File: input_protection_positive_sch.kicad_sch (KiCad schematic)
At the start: 26 parts, among them Q1 SQM120P06, Q2 SQM120P06, U1 ADM1270

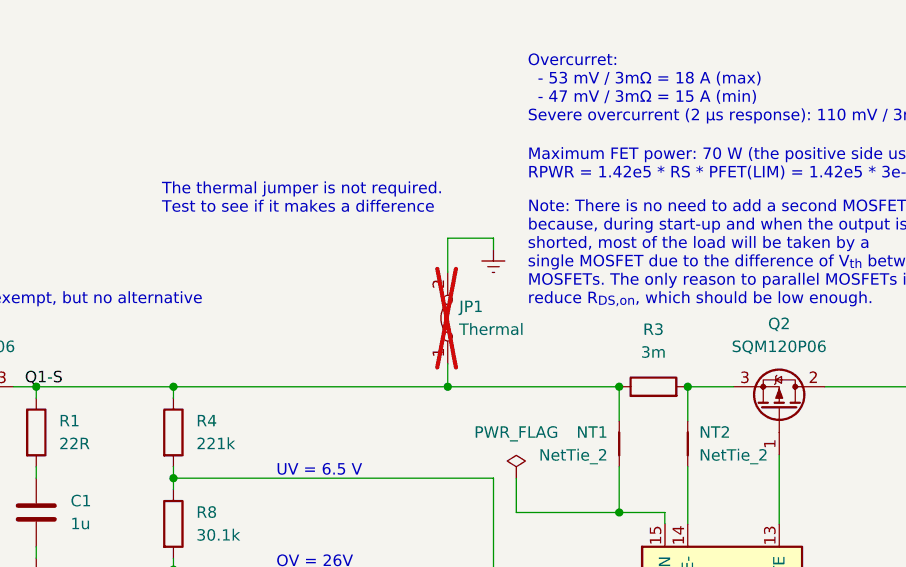
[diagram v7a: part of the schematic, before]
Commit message: Updated layout to improve handling flexing of the PCB Changed MLCCs to flexible termination Removed thermal jumper
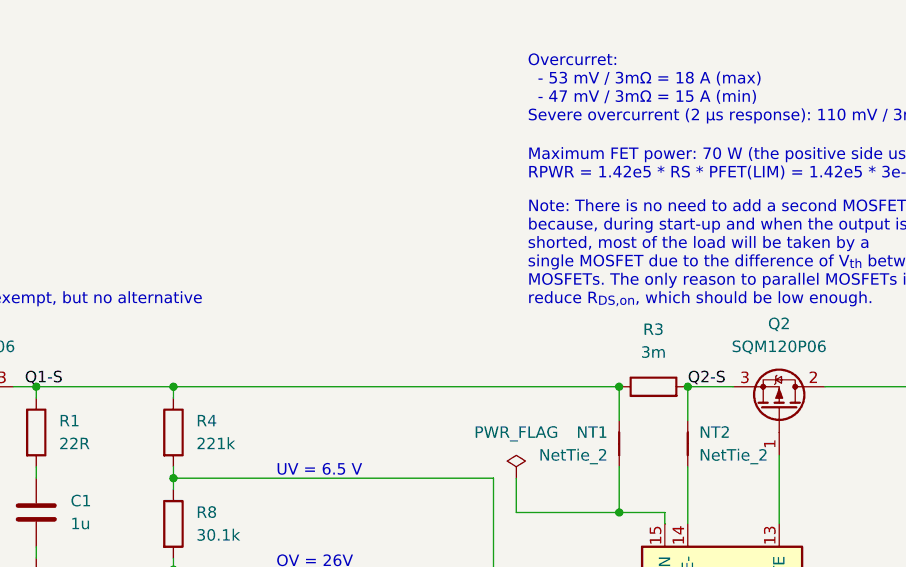
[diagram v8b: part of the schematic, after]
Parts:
- removed JP1: Thermal, Resistor_SMD:R_0612_1632Metric, symbol Jumper:Jumper_2_Bridged
- C1, C14, C15, C3: PN C1206C105K1RACAUTO -> C1206X105K1RACAUTO; digikey# 399-13374-1-ND -> 399-13377-1-ND
- C13: PN C1206C474K1RECAUTO -> C1206X474K1RECAUTO; digikey# 399-C1206C474K1RECAUTOCT-ND -> 399-16438-1-ND
- C2: PN C0805C104K1RACAUTO -> C0805X104K1RACAUTO; digikey# 399-6926-1-ND -> 399-11601-1-ND
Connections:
- net Q2-S: now reaches NT2.2, Q2.3 (S), R3.2
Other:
- note removed: "The thermal jumper is not required. Test to see if it makes a difference"
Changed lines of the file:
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@@
   (junction (at 27.94 64.77) (diameter 0) (color 0 0 0 0)
-  )
-  (junction (at 147.32 64.77) (diameter 0) (color 0 0 0 0)
   )
   (junction (at 163.83 97.79) (diameter 0) (color 0 0 0 0)
@@
     (stroke (width 0) (type default))
   )
-  (wire (pts (xy 116.84 64.77) (xy 147.32 64.77))
-    (stroke (width 0) (type default))
-  )
   (wire (pts (xy 45.72 64.77) (xy 45.72 67.31))
     (stroke (width 0) (type default))
   )
-  (wire (pts (xy 152.4 49.53) (xy 152.4 48.26))
-    (stroke (width 0) (type default))
-  )
   (wire (pts (xy 163.83 97.79) (xy 163.83 100.33))
     (stroke (width 0) (type default))
@@
     (stroke (width 0) (type default))
   )
-  (wire (pts (xy 152.4 48.26) (xy 147.32 48.26))
-    (stroke (width 0) (type default))
-  )
   (wire (pts (xy 245.11 64.77) (xy 259.08 64.77))
     (stroke (width 0) (type default))
@@
     (stroke (width 0) (type default))
   )
-  (wire (pts (xy 147.32 62.23) (xy 147.32 64.77))
-    (stroke (width 0) (type default))
-  )
   (wire (pts (xy 45.72 83.82) (xy 45.72 85.09))
     (stroke (width 0) (type default))
   )
-  (wire (pts (xy 147.32 64.77) (xy 166.37 64.77))
+  (wire (pts (xy 116.84 64.77) (xy 166.37 64.77))
     (stroke (width 0) (type default))
   )
@@
   )
   (wire (pts (xy 205.74 92.71) (xy 205.74 87.63))
-    (stroke (width 0) (type default))
-  )
-  (wire (pts (xy 147.32 48.26) (xy 147.32 52.07))
     (stroke (width 0) (type default))
   )
@@
     (effects (font (size 1.27 1.27)) (justify left bottom))
   )
-  (text "The thermal jumper is not required.\nTest to see if it makes a difference"
-    (at 115.57 45.72 0)
-    (effects (font (size 1.27 1.27)) (justify left bottom))
-  )
   (text "RoHS exempt, but no alternative" (at 91.44 55.88 0)
     (effects (font (size 1.27 1.27)) (justify left bottom))
@@
   )
   (label "Q1-D" (at 82.55 64.77 0) (fields_autoplaced)
+    (effects (font (size 1.27 1.27)) (justify left bottom))
+  )
+  (label "Q2-S" (at 173.99 64.77 0) (fields_autoplaced)
     (effects (font (size 1.27 1.27)) (justify left bottom))
   )
@@
       (effects (font (size 1.27 1.27)) hide)
     )
-    (property "PN" "C1206C105K1RACAUTO" (at 45.72 80.01 0)
+    (property "PN" "C1206X105K1RACAUTO" (at 45.72 80.01 0)
       (effects (font (size 1.27 1.27)) hide)
     )
@@
       (effects (font (size 1.27 1.27)) hide)
     )
-    (property "digikey#" "399-13374-1-ND" (at 45.72 80.01 0)
+    (property "digikey#" "399-13377-1-ND" (at 45.72 80.01 0)
       (effects (font (size 1.27 1.27)) hide)
     )
@@
       (effects (font (size 1.27 1.27)) hide)
     )
-    (property "PN" "C0805C104K1RACAUTO" (at 245.11 74.93 0)
+    (property "PN" "C0805X104K1RACAUTO" (at 245.11 74.93 0)
       (effects (font (size 1.27 1.27)) hide)
     )
@@
       (effects (font (size 1.27 1.27)) hide)
     )
-    (property "digikey#" "399-6926-1-ND" (at 245.11 74.93 0)
+    (property "digikey#" "399-11601-1-ND" (at 245.11 74.93 0)
       (effects (font (size 1.27 1.27)) hide)
     )
@@
     )
   )
-  (symbol (lib_id "power:Earth") (at 152.4 49.53 0) (unit 1)
-    (in_bom yes) (on_board yes) (dnp no) (fields_autoplaced)
-    (property "Reference" "#PWR070" (at 152.4 55.88 0)
-      (effects (font (size 1.27 1.27)) hide)
-    )
-    (property "Value" "Earth" (at 152.4 53.34 0)
-      (effects (font (size 1.27 1.27)) hide)
-    )
-    (property "Footprint" "" (at 152.4 49.53 0)
-      (effects (font (size 1.27 1.27)) hide)
-    )
-    (property "Datasheet" "~" (at 152.4 49.53 0)
-      (effects (font (size 1.27 1.27)) hide)
-    )
-    (pin "1")
-    (instances
-      (project "backplane"
-        (path "/b4ace06a-3ad4-479e-aaa4-d547ecf6903f/f9160387-088e-4a7b-8d58-b2647e07444c"
-          (reference "#PWR070") (unit 1)
-        )
-      )
-    )
-  )
   (symbol (lib_id "Device:R") (at 228.6 72.39 0) (unit 1)
     (in_bom yes) (on_board yes) (dnp no) (fields_autoplaced)
@@
       (effects (font (size 1.27 1.27)) hide)
     )
-    (property "PN" "C1206C105K1RACAUTO" (at 203.2 102.87 0)
+    (property "PN" "C1206X105K1RACAUTO" (at 203.2 102.87 0)
       (effects (font (size 1.27 1.27)) hide)
     )
@@
       (effects (font (size 1.27 1.27)) hide)
     )
-    (property "digikey#" "399-13374-1-ND" (at 203.2 102.87 0)
+    (property "digikey#" "399-13377-1-ND" (at 203.2 102.87 0)
       (effects (font (size 1.27 1.27)) hide)
     )
@@
       (effects (font (size 1.27 1.27)) hide)
     )
-    (property "PN" "C1206C105K1RACAUTO" (at 142.24 102.87 0)
+    (property "PN" "C1206X105K1RACAUTO" (at 142.24 102.87 0)
       (effects (font (size 1.27 1.27)) hide)
     )
@@
       (effects (font (size 1.27 1.27)) hide)
     )
-    (property "digikey#" "399-13374-1-ND" (at 142.24 102.87 0)
+    (property "digikey#" "399-13377-1-ND" (at 142.24 102.87 0)
       (effects (font (size 1.27 1.27)) hide)
     )
@@
       (effects (font (size 1.27 1.27)) hide)
     )
-    (property "PN" "C1206C474K1RECAUTO" (at 214.63 102.87 0)
+    (property "PN" "C1206X474K1RECAUTO" (at 214.63 102.87 0)
       (effects (font (size 1.27 1.27)) hide)
     )
@@
       (effects (font (size 1.27 1.27)) hide)
     )
-    (property "digikey#" "399-C1206C474K1RECAUTOCT-ND" (at 214.63 102.87 0)
+    (property "digikey#" "399-16438-1-ND" (at 214.63 102.87 0)
       (effects (font (size 1.27 1.27)) hide)
     )
@@
       (effects (font (size 1.27 1.27)) hide)
     )
-    (property "PN" "C1206C105K1RACAUTO" (at 101.6 78.74 0)
+    (property "PN" "C1206X105K1RACAUTO" (at 101.6 78.74 0)
       (effects (font (size 1.27 1.27)) hide)
     )
@@
       (effects (font (size 1.27 1.27)) hide)
     )
-    (property "digikey#" "399-13374-1-ND" (at 101.6 78.74 0)
+    (property "digikey#" "399-13377-1-ND" (at 101.6 78.74 0)
       (effects (font (size 1.27 1.27)) hide)
     )
@@
         )
       )
-    )
-  )
-  (symbol (lib_id "Jumper:Jumper_2_Bridged") (at 147.32 57.15 90) (unit 1)
-    (in_bom yes) (on_board yes) (dnp yes) (fields_autoplaced)
-    (property "Reference" "JP1" (at 148.59 55.88 90)
-      (effects (font (size 1.27 1.27)) (justify right))
-    )
-    (property "Value" "Thermal" (at 148.59 58.42 90)
-      (effects (font (size 1.27 1.27)) (justify right))
-    )
-    (property "Footprint" "Resistor_SMD:R_0612_1632Metric" (at 147.32 57.15 0)
-      (effects (font (size 1.27 1.27)) hide)
-    )
-    (property "Datasheet" "~" (at 147.32 57.15 0)
-      (effects (font (size 1.27 1.27)) hide)
-    )
-    (property "MFN" "Vishay" (at 147.32 57.15 0)
-      (effects (font (size 1.27 1.27)) hide)
-    )
-    (property "PN" "THJP0612AST1" (at 147.32 57.15 0)
-      (effects (font (size 1.27 1.27)) hide)
-    )
-    (property "RoHS" "Yes" (at 147.32 57.15 0)
-      (effects (font (size 1.27 1.27)) hide)
-    )
-    (property "Temperature" "Tstorage = –65 °C to 150 °C" (at 147.32 57.15 0)
-      (effects (font (size 1.27 1.27)) hide)
-    )
-    (pin "2")
-    (pin "1")
-    (instances
-      (project "backplane"
-        (path "/b4ace06a-3ad4-479e-aaa4-d547ecf6903f/f9160387-088e-4a7b-8d58-b2647e07444c"
-          (reference "JP1") (unit 1)
-        )
-      )
